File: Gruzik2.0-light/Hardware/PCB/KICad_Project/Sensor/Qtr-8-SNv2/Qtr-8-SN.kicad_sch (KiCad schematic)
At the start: 37 parts, among them Q1 NMOS

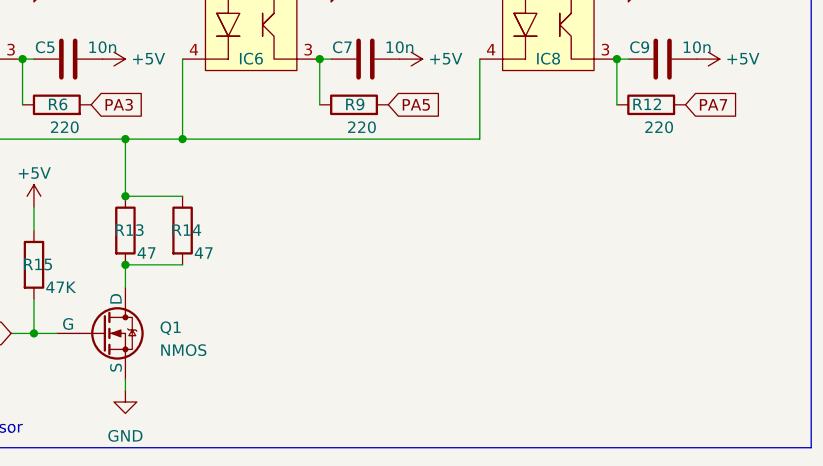
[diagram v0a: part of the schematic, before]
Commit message: 2.0.1
New sensor frame and upgraded software
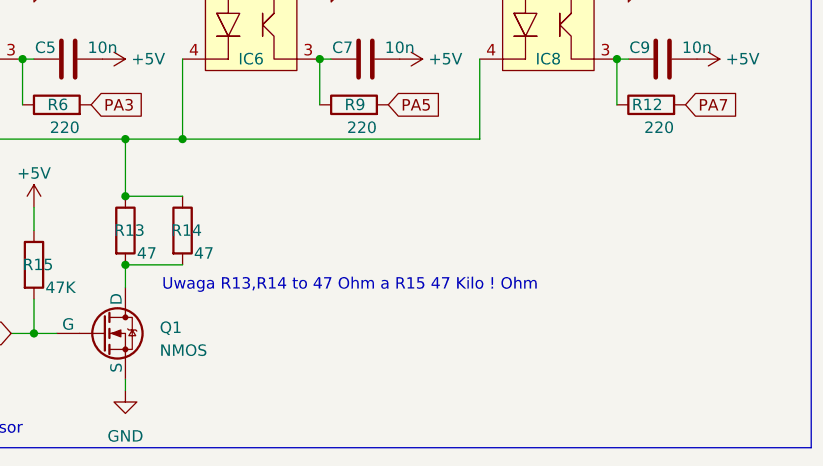
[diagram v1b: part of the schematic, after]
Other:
- note added: "Uwaga R13,R14 to 47 Ohm a R15 47 Kilo ! Ohm"
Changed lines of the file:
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@@
     (fill (type none))
+  )
+  (text "Uwaga R13,R14 to 47 Ohm a R15 47 Kilo ! Ohm" (at 84.074 127.508 0)
+    (effects (font (size 1.27 1.27)) (justify left bottom))
   )
   (text "Sensor connector" (at 16.51 17.78 0)
